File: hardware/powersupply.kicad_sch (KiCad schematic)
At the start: 15 parts, among them U1 h0536, U2 LD1117S33TR_SOT223

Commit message: done routing
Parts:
- removed C3: 470u, Capacitor_THT:CP_Radial_D8.0mm_P3.50mm, symbol Device:C_Polarized
- removed U1: h0536, Package_DIP:DIP-8_W7.62mm, symbol buck:h0536
- removed U2: LD1117S33TR_SOT223, Package_TO_SOT_SMD:SOT-223-3_TabPin2, symbol Regulator_Linear:LD1117S33TR_SOT223
- added C3: 100n, Capacitor_SMD:C_0603_1608Metric, symbol Device:C
- added R3: 10k, Resistor_SMD:R_0603_1608Metric, symbol Device:R
- added U2: LNK3202D, Package_SO:PowerIntegrations_SO-8C, symbol Regulator_Switching:LNK3202D
- C2: value 4u7 -> 22u
- L1: value 470u -> 1m
- R2: value 12k -> 4k
- R35: value 1k1 -> 2.49k
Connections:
- net +5V: now also L1.2; no longer L1.1
- net at D2.1 (K): now also C2.1, R2.1, R3.1; no longer R35.1
- net at R2.2, R35.2: now also U2.2 (FB)
- net at C2.2, D3.1 (K): now also L1.1, R35.1, C3.1, U2.5 (S), U2.6 (S), U2.7 (S), U2.8 (S); no longer L1.2, R2.1
- net at C14.1, L2.2: now also U2.4 (D)
- new net: C3.2, R3.2, U2.1 (BP/M)
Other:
- moved on the sheet: C1, C14, C2, C4, D1, D2, D3, L1, L2, R1, R2, R35

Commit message: bugfix: triac output needs to confront L potential
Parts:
- R1: footprint Resistor_SMD:R_1206_3216Metric -> Resistor_SMD:R_2512_6332Metric
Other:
- moved on the sheet: L1
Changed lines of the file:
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@@
-	)
-	(junction
-		(at 170.18 86.36)
-		(diameter 0)
-		(color 0 0 0 0)
 	)
 	(junction
@@
 	)
 	(junction
+		(at 163.83 104.14)
+		(diameter 0)
+		(color 0 0 0 0)
+	)
+	(junction
 		(at 184.15 104.14)
 		(diameter 0)
@@
 	)
 	(junction
-		(at 170.18 104.14)
-		(diameter 0)
-		(color 0 0 0 0)
-	)
-	(junction
 		(at 138.43 104.14)
 		(diameter 0)
@@
 	(wire
 		(pts
-			(xy 170.18 99.06) (xy 170.18 104.14)
-		)
-		(stroke
-			(width 0)
-			(type default)
-		)
-	)
-	(wire
-		(pts
-			(xy 138.43 104.14) (xy 170.18 104.14)
-		)
-		(stroke
-			(width 0)
-			(type default)
-		)
-	)
-	(wire
-		(pts
-			(xy 170.18 86.36) (xy 170.18 91.44)
+			(xy 163.83 99.06) (xy 163.83 104.14)
+		)
+		(stroke
+			(width 0)
+			(type default)
+		)
+	)
+	(wire
+		(pts
+			(xy 138.43 104.14) (xy 163.83 104.14)
+		)
+		(stroke
+			(width 0)
+			(type default)
+		)
+	)
+	(wire
+		(pts
+			(xy 163.83 104.14) (xy 184.15 104.14)
+		)
+		(stroke
+			(width 0)
+			(type default)
+		)
+	)
+	(wire
+		(pts
+			(xy 163.83 86.36) (xy 163.83 91.44)
 		)
 		(stroke
@@
 	(wire
 		(pts
-			(xy 170.18 86.36) (xy 176.53 86.36)
+			(xy 163.83 86.36) (xy 176.53 86.36)
 		)
 		(stroke
@@
 	(wire
 		(pts
-			(xy 170.18 104.14) (xy 184.15 104.14)
-		)
-		(stroke
-			(width 0)
-			(type default)
-		)
-	)
-	(wire
-		(pts
 			(xy 138.43 86.36) (xy 142.24 86.36)
 		)
@@
 		(pts
 			(xy 128.27 86.36) (xy 125.73 86.36)
-		)
-		(stroke
-			(width 0)
-			(type default)
-		)
-	)
-	(wire
-		(pts
-			(xy 163.83 86.36) (xy 170.18 86.36)
 		)
 		(stroke
@@
 		(dnp no)
 		(property "Reference" "R35"
-			(at 181.61 84.328 90)
+			(at 181.61 88.646 90)
 			(effects
 				(font
@@
 		(dnp no)
 		(property "Reference" "R2"
-			(at 189.23 84.328 90)
+			(at 189.23 88.646 90)
 			(effects
 				(font
@@
 	(symbol
 		(lib_id "Device:L")
-		(at 170.18 95.25 0)
+		(at 163.83 95.25 0)
 		(unit 1)
 		(exclude_from_sim no)
@@
 		(dnp no)
 		(property "Reference" "L1"
-			(at 172.212 95.25 90)
+			(at 165.862 95.25 90)
 			(effects
 				(font
@@
 		)
 		(property "Value" "1m"
-			(at 168.91 95.25 90)
+			(at 162.56 95.25 90)
 			(effects
 				(font
@@
 		)
 		(property "Footprint" "Inductor_THT:L_Radial_D10.0mm_P5.00mm_Fastron_07P"
-			(at 170.18 95.25 0)
+			(at 163.83 95.25 0)
 			(effects
 				(font
@@
 		)
 		(property "Datasheet" "~"
-			(at 170.18 95.25 0)
+			(at 163.83 95.25 0)
 			(effects
 				(font
@@
 		)
 		(property "Description" ""
-			(at 170.18 95.25 0)
+			(at 163.83 95.25 0)
 			(effects
 				(font
@@
 			)
 		)
-		(property "Footprint" "Resistor_SMD:R_1206_3216Metric"
+		(property "Footprint" "Resistor_SMD:R_2512_6332Metric"
 			(at 110.49 88.138 90)
 			(effects

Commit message: added some datasheets
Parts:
- added C5: 220u, Capacitor_THT:CP_Radial_D8.0mm_P3.50mm, symbol Device:C_Polarized
- added L3: 1m, Inductor_SMD:L_Wuerth_WE-XHMI-8080, symbol Device:L
- L1: footprint Inductor_THT:L_Radial_D10.0mm_P5.00mm_Fastron_07P -> Inductor_SMD:L_Wuerth_WE-XHMI-8080
- L2: value 2.2mH -> 1m; footprint Inductor_THT:L_Axial_L7.0mm_D3.3mm_P12.70mm_Horizontal_Fastron_MICC -> Inductor_SMD:L_Wuerth_WE-XHMI-8080
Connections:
- net +5V: now also C5.1, L3.2; no longer C1.2, C14.2, C4.1, D2.2 (A), L1.2
- net GND: now also C5.2
- new net AC_N: C1.2, C14.2, C4.1, D2.2 (A), L1.2, L3.1
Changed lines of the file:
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@@
+	)
+	(junction
+		(at 210.82 104.14)
+		(diameter 0)
+		(color 0 0 0 0)
+	)
+	(junction
+		(at 210.82 114.3)
+		(diameter 0)
+		(color 0 0 0 0)
 	)
 	(junction
@@
 	(wire
 		(pts
+			(xy 210.82 104.14) (xy 210.82 105.41)
+		)
+		(stroke
+			(width 0)
+			(type default)
+		)
+	)
+	(wire
+		(pts
 			(xy 194.31 91.44) (xy 194.31 86.36)
 		)
@@
 	(wire
 		(pts
+			(xy 210.82 104.14) (xy 217.17 104.14)
+		)
+		(stroke
+			(width 0)
+			(type default)
+		)
+	)
+	(wire
+		(pts
 			(xy 194.31 86.36) (xy 194.31 78.74)
 		)
@@
 	(wire
 		(pts
+			(xy 194.31 104.14) (xy 199.39 104.14)
+		)
+		(stroke
+			(width 0)
+			(type default)
+		)
+	)
+	(wire
+		(pts
 			(xy 163.83 104.14) (xy 184.15 104.14)
 		)
@@
 	(wire
 		(pts
-			(xy 184.15 114.3) (xy 200.66 114.3)
+			(xy 210.82 114.3) (xy 217.17 114.3)
 		)
 		(stroke
@@
 	(wire
 		(pts
+			(xy 184.15 114.3) (xy 210.82 114.3)
+		)
+		(stroke
+			(width 0)
+			(type default)
+		)
+	)
+	(wire
+		(pts
 			(xy 149.86 74.93) (xy 185.42 74.93)
 		)
@@
 	(wire
 		(pts
+			(xy 207.01 104.14) (xy 210.82 104.14)
+		)
+		(stroke
+			(width 0)
+			(type default)
+		)
+	)
+	(wire
+		(pts
 			(xy 162.56 86.36) (xy 163.83 86.36)
 		)
@@
 	(wire
 		(pts
+			(xy 210.82 113.03) (xy 210.82 114.3)
+		)
+		(stroke
+			(width 0)
+			(type default)
+		)
+	)
+	(wire
+		(pts
 			(xy 163.83 78.74) (xy 166.37 78.74)
 		)
@@
 		(pts
 			(xy 104.14 86.36) (xy 106.68 86.36)
-		)
-		(stroke
-			(width 0)
-			(type default)
-		)
-	)
-	(wire
-		(pts
-			(xy 194.31 104.14) (xy 200.66 104.14)
 		)
 		(stroke
@@
 	(hierarchical_label "GND"
 		(shape input)
-		(at 200.66 114.3 0)
+		(at 217.17 114.3 0)
 		(fields_autoplaced yes)
 		(effects
@@
 	(hierarchical_label "+5V"
 		(shape input)
-		(at 200.66 104.14 0)
+		(at 217.17 104.14 0)
 		(fields_autoplaced yes)
 		(effects
@@
 			)
 		)
-		(property "Footprint" "Inductor_THT:L_Radial_D10.0mm_P5.00mm_Fastron_07P"
+		(property "Footprint" "Inductor_SMD:L_Wuerth_WE-XHMI-8080"
 			(at 163.83 95.25 0)
 			(effects
@@
 			)
 		)
-		(property "Value" "2.2mH"
+		(property "Value" "1m"
 			(at 132.08 87.63 90)
 			(effects
@@
 			)
 		)
-		(property "Footprint" "Inductor_THT:L_Axial_L7.0mm_D3.3mm_P12.70mm_Horizontal_Fastron_MICC"
+		(property "Footprint" "Inductor_SMD:L_Wuerth_WE-XHMI-8080"
 			(at 132.08 86.36 0)
 			(effects
@@
 				(path "/ae153005-c1c4-4678-92de-98a47cf88e8d/c42b7df1-fc74-4864-a9e3-b6ebdfdb24fb"
 					(reference "C2")
+					(unit 1)
+				)
+			)
+		)
+	)
+	(symbol
+		(lib_id "Device:C_Polarized")
+		(at 210.82 109.22 0)
+		(unit 1)
+		(exclude_from_sim no)
+		(in_bom yes)
+		(on_board yes)
+		(dnp no)
+		(fields_autoplaced yes)
+		(property "Reference" "C5"
+			(at 214.63 107.0609 0)
+			(effects
+				(font
+					(size 1.27 1.27)
+				)
+				(justify left)
+			)
+		)
+		(property "Value" "220u"
+			(at 214.63 109.6009 0)
+			(effects
+				(font
+					(size 1.27 1.27)
+				)
+				(justify left)
+			)
+		)
+		(property "Footprint" "Capacitor_THT:CP_Radial_D8.0mm_P3.50mm"
+			(at 211.7852 113.03 0)
+			(effects
+				(font
+					(size 1.27 1.27)
+				)
+				(hide yes)
+			)
+		)
+		(property "Datasheet" "~"
+			(at 210.82 109.22 0)
+			(effects
+				(font
+					(size 1.27 1.27)
+				)
+				(hide yes)
+			)
+		)
+		(property "Description" ""
+			(at 210.82 109.22 0)
+			(effects
+				(font
+					(size 1.27 1.27)
+				)
+				(hide yes)
+			)
+		)
+		(pin "1"
+		)
+		(pin "2"
+		)
+		(instances
+			(project "Steuerplatine"
+				(path "/ae153005-c1c4-4678-92de-98a47cf88e8d/c42b7df1-fc74-4864-a9e3-b6ebdfdb24fb"
+					(reference "C5")
 					(unit 1)
 				)
@@
 					(unit 1)
 				)
+			)
+		)
+	)
+	(symbol
+		(lib_id "Device:L")
+		(at 203.2 104.14 90)
+		(unit 1)
+		(exclude_from_sim no)
+		(in_bom yes)
+		(on_board yes)
+		(dnp no)
+		(property "Reference" "L3"
+			(at 200.66 101.6 90)
+			(effects
+				(font
+					(size 1.27 1.27)
+				)
+			)
+		)
+		(property "Value" "1m"
+			(at 203.2 105.41 90)
+			(effects
+				(font
+					(size 1.27 1.27)
+				)
+			)
+		)
+		(property "Footprint" "Inductor_SMD:L_Wuerth_WE-XHMI-8080"
+			(at 203.2 104.14 0)
+			(effects
+				(font
+					(size 1.27 1.27)
+				)
+				(hide yes)
+			)
+		)
+		(property "Datasheet" "~"
+			(at 203.2 104.14 0)
+			(effects
+				(font
+					(size 1.27 1.27)
+				)
+				(hide yes)
+			)
+		)
+		(property "Description" ""
+			(at 203.2 104.14 0)
+			(effects
+				(font
+					(size 1.27 1.27)
+				)
+				(hide yes)
+			)
+		)
+		(pin "1"
+		)
+		(pin "2"
+		)
+		(instances
+			(project "Steuerplatine"
+				(path "/ae153005-c1c4-4678-92de-98a47cf88e8d/c42b7df1-fc74-4864-a9e3-b6ebdfdb24fb"
+					(reference "L3")
+					(unit 1)
+				)

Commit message: changed capacitors to smd
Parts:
- C1, C14: footprint Capacitor_THT:CP_Radial_D8.0mm_P3.80mm -> Capacitor_SMD:CP_Elec_8x10
- C4, C5: value 220u -> 100u; footprint Capacitor_THT:CP_Radial_D8.0mm_P3.50mm -> Capacitor_SMD:CP_Elec_6.3x3
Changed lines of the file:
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@@
 			)
 		)
-		(property "Footprint" "Capacitor_THT:CP_Radial_D8.0mm_P3.80mm"
+		(property "Footprint" "Capacitor_SMD:CP_Elec_8x10"
 			(at 139.3952 99.06 0)
 			(effects
@@
 			)
 		)
-		(property "Value" "220u"
+		(property "Value" "100u"
 			(at 214.63 109.6009 0)
 			(effects
@@
 			)
 		)
-		(property "Footprint" "Capacitor_THT:CP_Radial_D8.0mm_P3.50mm"
+		(property "Footprint" "Capacitor_SMD:CP_Elec_6.3x3"
 			(at 211.7852 113.03 0)
 			(effects
@@
 			)
 		)
-		(property "Value" "220u"
+		(property "Value" "100u"
 			(at 187.96 109.6009 0)
 			(effects
@@
 			)
 		)
-		(property "Footprint" "Capacitor_THT:CP_Radial_D8.0mm_P3.50mm"
+		(property "Footprint" "Capacitor_SMD:CP_Elec_6.3x3"
 			(at 185.1152 113.03 0)
 			(effects
@@
 			)
 		)
-		(property "Footprint" "Capacitor_THT:CP_Radial_D8.0mm_P3.80mm"
+		(property "Footprint" "Capacitor_SMD:CP_Elec_8x10"
 			(at 126.6952 99.06 0)
 			(effects

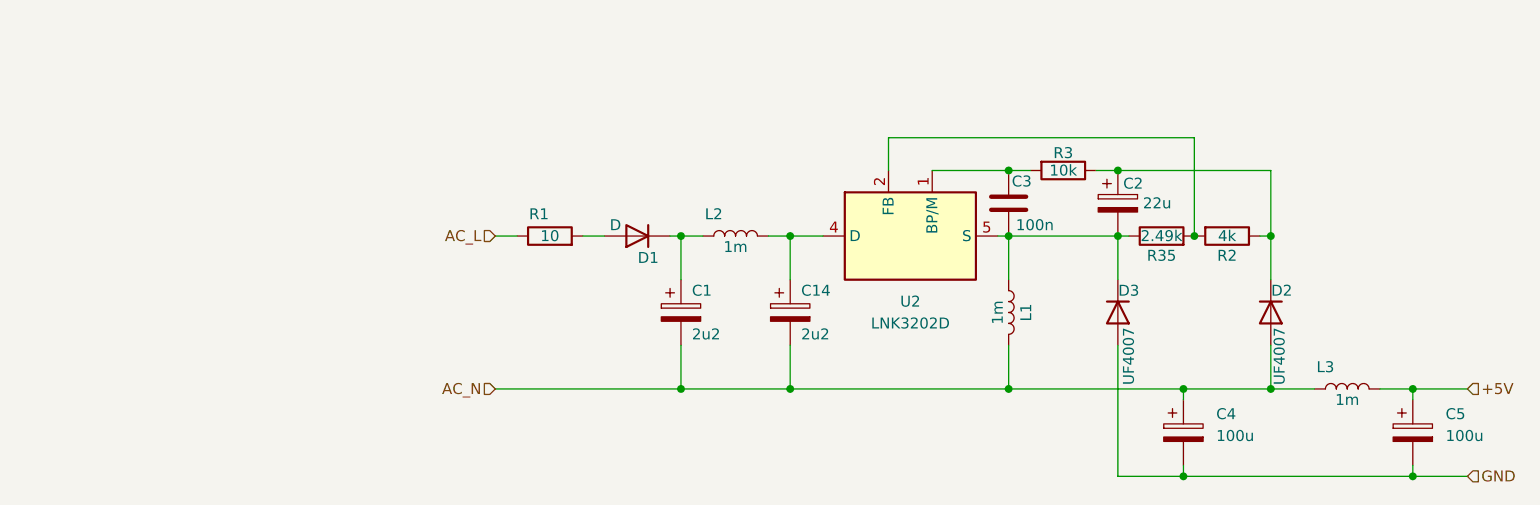
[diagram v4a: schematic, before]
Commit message: changed diodes footprint
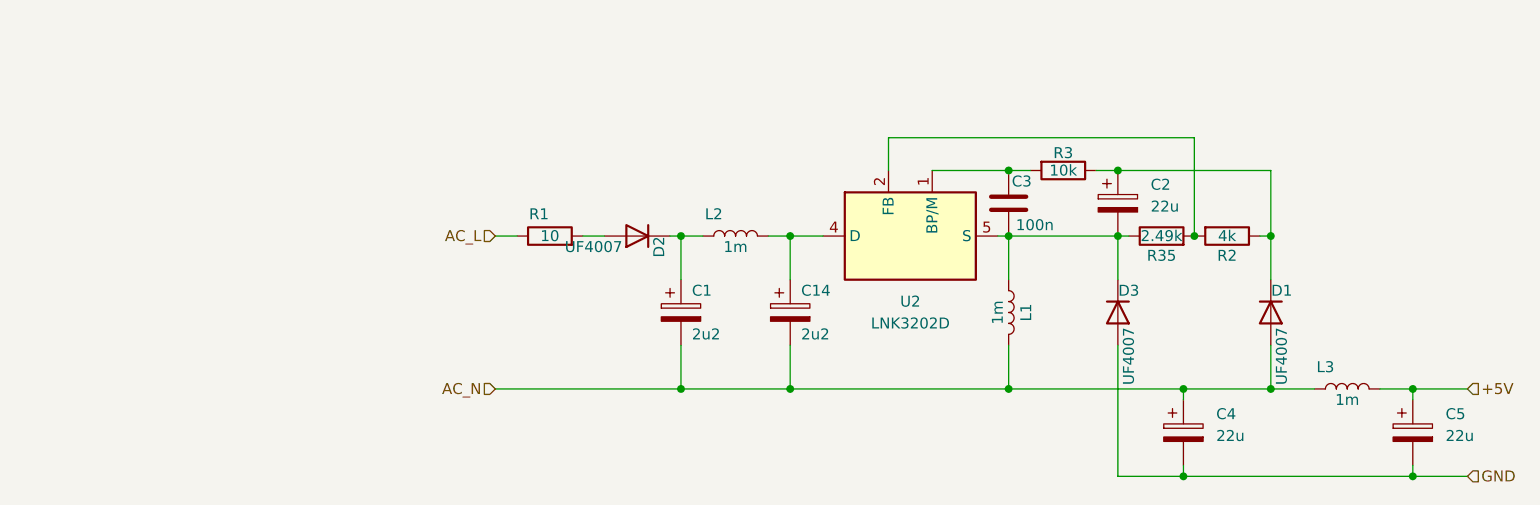
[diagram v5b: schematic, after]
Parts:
- C2: footprint Capacitor_THT:CP_Radial_D5.0mm_P2.50mm -> Capacitor_SMD:CP_Elec_6.3x3
- C4, C5: value 100u -> 22u
- D1: value D -> UF4007; footprint Diode_SMD:D_SMA_Handsoldering -> Diode_SMD:D_SMB
- D2, D3: footprint Diode_SMD:D_SMA_Handsoldering -> Diode_SMD:D_SMB
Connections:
- net AC_N: now also D1.2 (A); no longer D2.2 (A)
- net at C2.1, R2.1, R3.1: now also D1.1 (K); no longer D2.1 (K)
- net at C1.1, L2.1: now also D2.1 (K); no longer D1.1 (K)
- net at R1.2: now also D2.2 (A); no longer D1.2 (A)

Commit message: changed some parts to stuff you can actually order
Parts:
- R1: footprint Resistor_SMD:R_2512_6332Metric -> Resistor_SMD:R_2816_7142Metric
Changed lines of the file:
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@@
 			)
 		)
-		(property "Footprint" "Resistor_SMD:R_2512_6332Metric"
+		(property "Footprint" "Resistor_SMD:R_2816_7142Metric"
 			(at 110.49 88.138 90)
 			(effects
